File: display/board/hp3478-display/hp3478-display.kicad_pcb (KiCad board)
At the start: 2 copper layers, 130.2 x 29.8 mm, 242 parts, among them J1 SFV10R-1ST, J2 DNP, U1 PIC16F15274-I/MP, U2 DNP

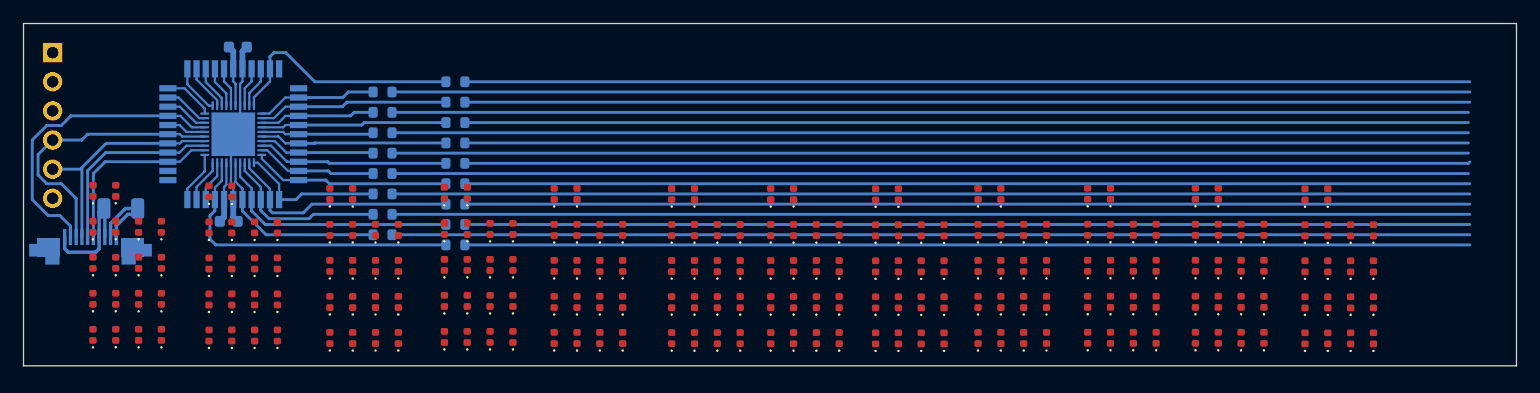
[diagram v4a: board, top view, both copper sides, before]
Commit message: Add digit outlines and place LEDs.
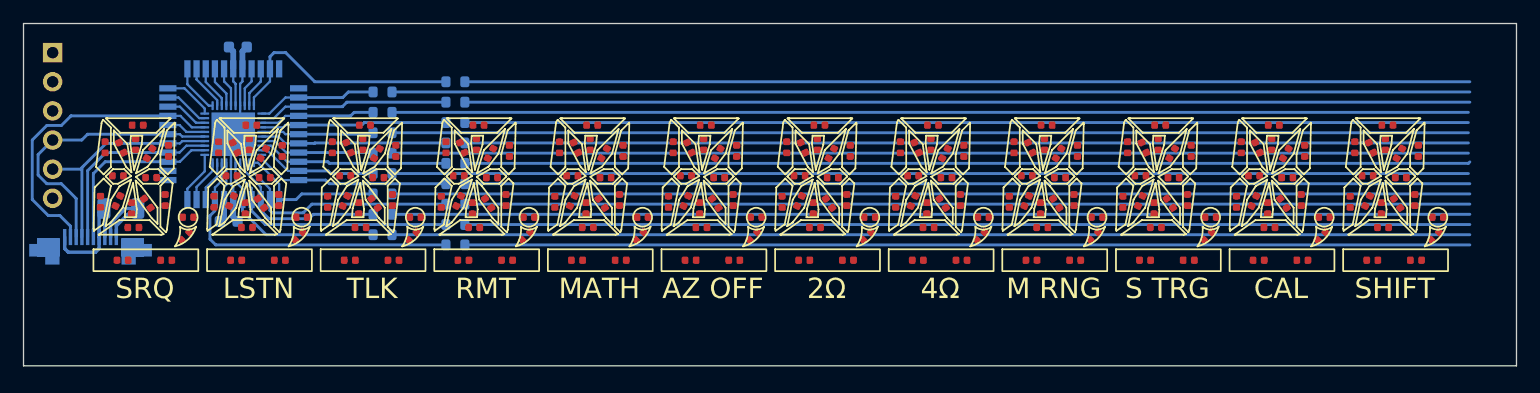
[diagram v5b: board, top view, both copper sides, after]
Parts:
- added REF**: Value, 0Local:Digit_Outline, F.Cu at (82.3, 69.2)
- added REF**1: Value, 0Local:Digit_Outline, F.Cu at (92.2, 69.2)
- added REF**10: Value, 0Local:Digit_Outline, F.Cu at (181.4, 69.2)
- added REF**11: Value, 0Local:Digit_Outline, F.Cu at (191.3, 69.2)
- added REF**2: Value, 0Local:Digit_Outline, F.Cu at (102.1, 69.2)
- added REF**3: Value, 0Local:Digit_Outline, F.Cu at (112.0, 69.2)
- added REF**4: Value, 0Local:Digit_Outline, F.Cu at (121.9, 69.2)
- added REF**5: Value, 0Local:Digit_Outline, F.Cu at (131.8, 69.2)
- added REF**6: Value, 0Local:Digit_Outline, F.Cu at (141.7, 69.2)
- added REF**7: Value, 0Local:Digit_Outline, F.Cu at (151.6, 69.2)
- added REF**8: Value, 0Local:Digit_Outline, F.Cu at (161.5, 69.2)
- added REF**9: Value, 0Local:Digit_Outline, F.Cu at (171.4, 69.2)
- D1001, D1002, D1003, D1004, D1005, D1006, D1007, D1008, D1009, D1010, D1011, D1012, D1013, D1014, D1015, D1016, D1017, D1018, D1101, D1102, D1103, D1104, D1105, D1106, D1107, D1108, D1109, D1110, D1111, D1112, D1113, D1114, D1115, D1116, D1117, D1118, D1201, D1202, D1203, D1204, D1205, D1206, D1207, D1208, D1209, D1210, D1211, D1212, D1213, D1214, D1215, D1216, D1217, D1218, D1301, D1302, D1303, D1304, D1305, D1306, D1307, D1308, D1309, D1310, D1311, D1312, D1313, D1314, D1315, D1316, D1317, D1318, D201, D202, D203, D204, D205, D206, D207, D208, D209, D210, D211, D212, D213, D214, D215, D216, D217, D218, D301, D302, D303, D304, D305, D306, D307, D308, D309, D310, D311, D312, D313, D314, D315, D316, D317, D318, D401, D402, D403, D404, D405, D406, D407, D408, D409, D410, D411, D412, D413, D414, D415, D416, D417, D418, D501, D502, D503, D504, D505, D506, D507, D508, D509, D510, D511, D512, D513, D514, D515, D516, D517, D518, D601, D602, D603, D604, D605, D606, D607, D608, D609, D610, D611, D612, D613, D614, D615, D616, D617, D618, D701, D702, D703, D704, D705, D706, D707, D708, D709, D710, D711, D712, D713, D714, D715, D716, D717, D718, D801, D802, D803, D804, D805, D806, D807, D808, D809, D810, D811, D812, D813, D814, D815, D816, D817, D818, D901, D902, D903, D904, D905, D906, D907, D908, D909, D910, D911, D912, D913, D914, D915, D916, D917, D918: footprint LED_SMD:LED_0402_1005Metric -> 0Local:LED_0402_1005Metric
- moved D1301 19.9 mm to (195.1, 59.7), turned to 180 degrees
- moved D1201 19.8 mm to (185.2, 59.7), turned to 180 degrees
- moved D1101 19.6 mm to (175.3, 59.7), turned to 180 degrees
- moved D1001 19.5 mm to (165.4, 59.7), turned to 180 degrees
- moved D901 19.3 mm to (155.5, 59.7), turned to 180 degrees
- moved D801 19.0 mm to (145.6, 59.7), turned to 180 degrees
- moved D601 18.8 mm to (125.8, 59.7), turned to 180 degrees
- moved D401 18.8 mm to (106.0, 59.7), turned to 180 degrees
- moved D701 18.8 mm to (135.7, 59.7), turned to 180 degrees
- moved D301 18.7 mm to (96.1, 59.7), turned to 180 degrees
- moved D501 18.7 mm to (115.9, 59.7), turned to 180 degrees
- moved D201 18.7 mm to (86.2, 59.7), turned to 180 degrees
- moved D1302 16.8 mm to (192.3, 61.6)
- moved D702 16.7 mm to (132.8, 61.6)
- moved D1202 16.7 mm to (182.4, 61.6)
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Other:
- board text added: "2Ω"
- board text added: "4Ω"
- board text added: "AZ OFF"
- board text added: "CAL"
- board text added: "LSTN"
- board text added: "M RNG"
- board text added: "MATH"
- board text added: "RMT"
- board text added: "S TRG"
- board text added: "SHIFT"
- board text added: "SRQ"
- board text added: "TLK"

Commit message: Route LED anode bus.
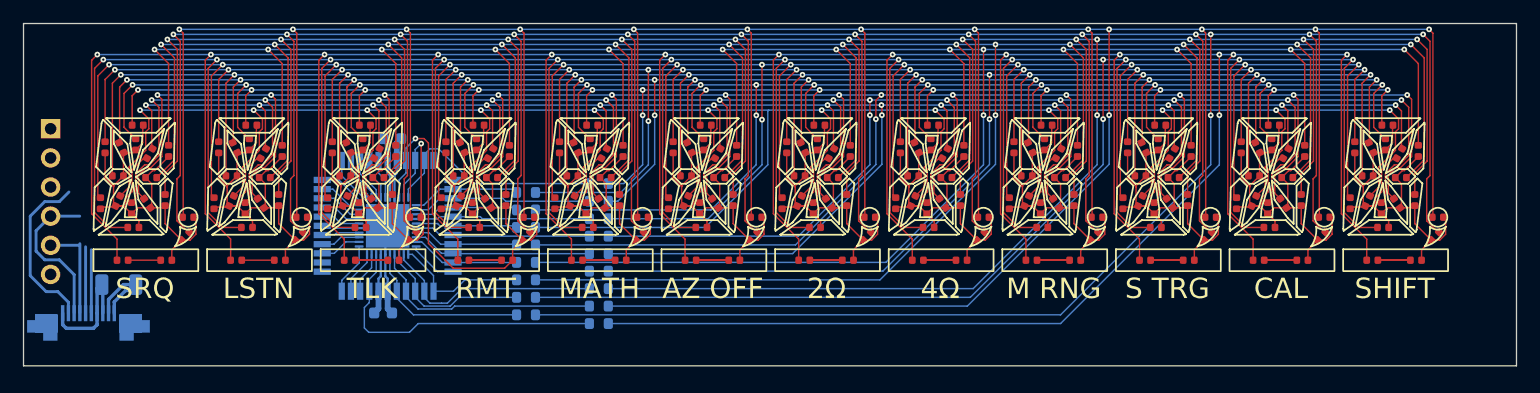
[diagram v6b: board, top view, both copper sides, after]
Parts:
- moved C2 15.7 mm to (108.3, 60.8)
- moved C3 15.7 mm to (107.5, 76.0)
- moved U1 15.7 mm to (108.0, 68.4)
- moved U2 15.7 mm to (108.0, 68.4)
- moved R10 15.3 mm to (126.4, 64.8)
- moved R11 15.3 mm to (120.0, 65.5)
- moved R12 15.2 mm to (126.4, 66.3)
- moved R13 15.1 mm to (120.0, 67.1)
- moved R18 15.1 mm to (126.4, 67.8)
- moved R19 15.0 mm to (120.0, 68.6)
- moved R20 14.9 mm to (126.4, 69.3)
- moved R21 14.8 mm to (120.0, 70.1)
- moved R14 14.8 mm to (126.4, 70.9)
- moved R15 14.7 mm to (120.0, 71.6)
- moved R16 14.6 mm to (126.4, 72.4)
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- renumbered REF** to REF0, REF**1 to REF1, REF**10 to REF10, REF**11 to REF11, REF**2 to REF2, REF**3 to REF3, REF**4 to REF4, REF**5 to REF5, REF**6 to REF6, REF**7 to REF7, REF**8 to REF8, REF**9 to REF9
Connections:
- U1 pad 20: /K2 -> /K5
- U1 pad 21: /K3 -> /K6
- U1 pad 28: /K6 -> /K3
- U1 pad 29: /K5 -> /K2
- U2 pad 22: /K2 -> /K5
- U2 pad 23: /K3 -> /K6
- U2 pad 30: /K6 -> /K3
- U2 pad 31: /K5 -> /K2
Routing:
- net /A16: track 87.6 -> 406.2 mm, vias 0 -> 14
- net /A15: track 94.0 -> 402.1 mm, vias 0 -> 14
- net /A13: track 94.0 -> 377.4 mm, vias 0 -> 14
- net /A14: track 87.6 -> 368.1 mm, vias 0 -> 14
- net /A12: track 87.6 -> 338.8 mm, vias 0 -> 14
- net /A7: track 94.0 -> 316.5 mm, vias 0 -> 14
- net /A8: track 87.5 -> 278.3 mm, vias 0 -> 14
- net /A11: track 93.9 -> 273.7 mm, vias 0 -> 14
- net /A10: track 87.5 -> 265.4 mm, vias 0 -> 14
- net /A6: track 87.6 -> 263.3 mm, vias 0 -> 14
- net /A5: track 93.9 -> 267.9 mm, vias 0 -> 14
- net /A9: track 93.9 -> 242.2 mm, vias 0 -> 12
- net /A1: track 94.0 -> 207.7 mm, vias 0 -> 14
- net /A3: track 93.9 -> 202.1 mm, vias 0 -> 14
- net /A2: track 87.6 -> 190.8 mm, vias 0 -> 14
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
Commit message: Route LED cathode nets.
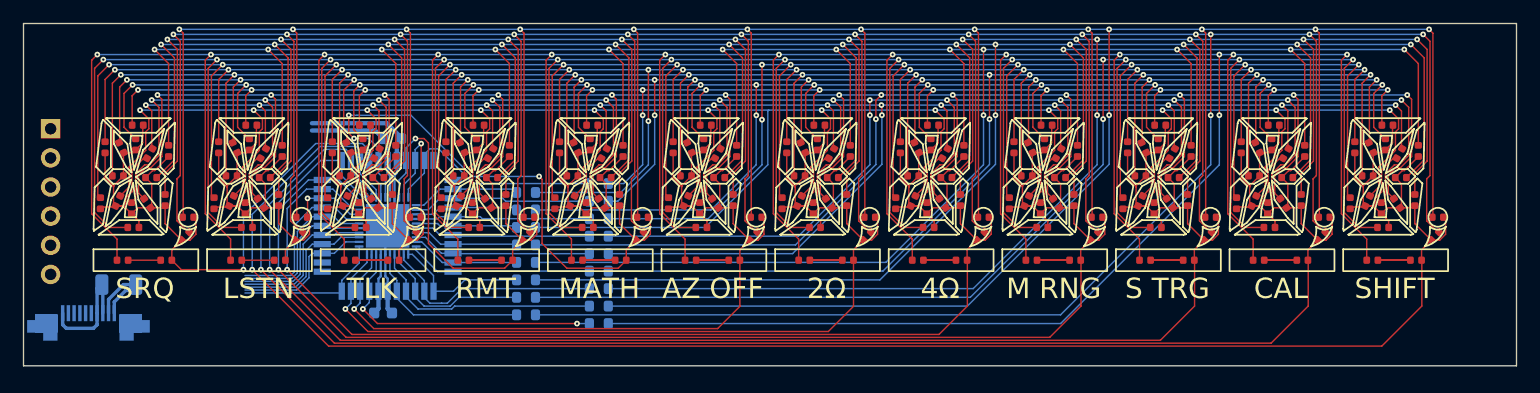
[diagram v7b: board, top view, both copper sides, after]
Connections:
- J2 pad 6: unconnected-(J2-Pad6) -> /DBG
- U1 pad 10: /K8 -> /K6
- U1 pad 11: Net-(U1-Pad11) -> /DBG
- U1 pad 18: /K0 -> /K1
- U1 pad 19: /K1 -> /K7
- U1 pad 20: /K5 -> /K8
- U1 pad 21: /K6 -> /K9
- U1 pad 22: /K4 -> /K10
- U1 pad 23: /K9 -> /K11
- U1 pad 24: /K10 -> /K0
- U1 pad 25: /K11 -> /K4
- U1 pad 9: /K7 -> /K5
- U2 pad 10: /K8 -> /K6
- U2 pad 11: Net-(U1-Pad11) -> /DBG
- U2 pad 20: /K0 -> /K1
- U2 pad 21: /K1 -> /K7
- U2 pad 22: /K5 -> /K8
- U2 pad 23: /K6 -> /K9
- U2 pad 24: /K4 -> /K10
- U2 pad 25: /K9 -> /K11
- U2 pad 26: /K10 -> /K0
- U2 pad 27: /K11 -> /K4
- U2 pad 9: /K7 -> /K5
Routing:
- net /K11: track 43.5 -> 171.7 mm, vias 0 -> 1
- net /K10: track 43.6 -> 159.1 mm, vias 0 -> 1
- net /K9: track 43.8 -> 146.0 mm, vias 0 -> 1
- net /K8: track 43.8 -> 132.1 mm, vias 0 -> 1
- net /K7: track 43.6 -> 119.7 mm, vias 0 -> 1
- net /K6: track 44.3 -> 95.6 mm, vias 0 -> 1
- net /K5: track 44.4 -> 84.5 mm, vias 0 -> 1
- net /K4: track 44.0 -> 82.6 mm, vias 0 -> 3
- net /K0: track 44.0 -> 69.6 mm, vias 0 -> 1
- net /DBG: track 0.00 -> 13.0 mm
- net /HA6: track 4.32 -> 16.2 mm
- net /~{MCLR}: track 3.46 -> 14.6 mm
- net GND: track 24.8 -> 33.0 mm
- net +5V: track 18.4 -> 24.9 mm
- net Net-(U1-Pad11): track 4.53 -> 0.00 mm
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
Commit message: Route inputs and MCU support nets.
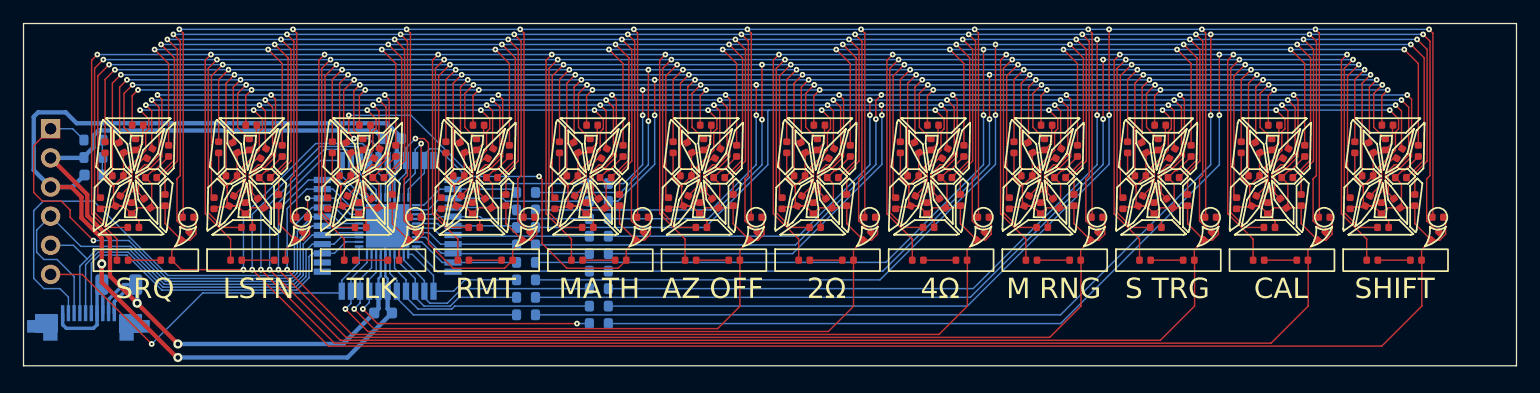
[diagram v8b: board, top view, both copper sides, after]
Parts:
- added C4: 10n, Capacitor_SMD:C_0603_1608Metric, B.Cu at (82.3, 64.0)
- added R1: 10k, Resistor_SMD:R_0603_1608Metric, B.Cu at (82.3, 62.5)
- added R2: 470R, Resistor_SMD:R_0603_1608Metric, B.Cu at (82.3, 61.0)
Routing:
- net GND: track 33.0 -> 110.6 mm, vias 0 -> 2
- net +5V: track 24.9 -> 89.9 mm, vias 0 -> 2
- net /PWO: track 15.2 -> 47.7 mm
- net /~{MCLR}: track 14.6 -> 45.9 mm, vias 0 -> 1
- net /PGD/IWA: track 13.9 -> 44.2 mm
- net /PGC/ISA: track 13.4 -> 37.5 mm
- net /DBG: track 13.0 -> 34.3 mm, vias 0 -> 1
- net /SYNC: track 13.1 -> 32.9 mm
- net /P1: track 12.8 -> 32.1 mm
- net Net-(C4-Pad1): track 0.00 -> 3.07 mm
- net Net-(D817-Pad1): track 5.68 -> 2.84 mm
- net Net-(D717-Pad1): track 5.68 -> 2.84 mm
- net Net-(D617-Pad1): track 5.68 -> 2.84 mm
- net Net-(D517-Pad1): track 5.68 -> 2.84 mm
- net Net-(D417-Pad1): track 5.68 -> 2.84 mm
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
